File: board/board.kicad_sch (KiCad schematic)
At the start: 10 parts, among them J1 RJ12, J10 PLAN, J2 JST XH, J3 JST XH, J4 RJ12, J5 Barrel_Jack, J6 Seriale, J7 MPX, J8 Conn_02x10_Counter_Clockwise_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, J9 Seriale

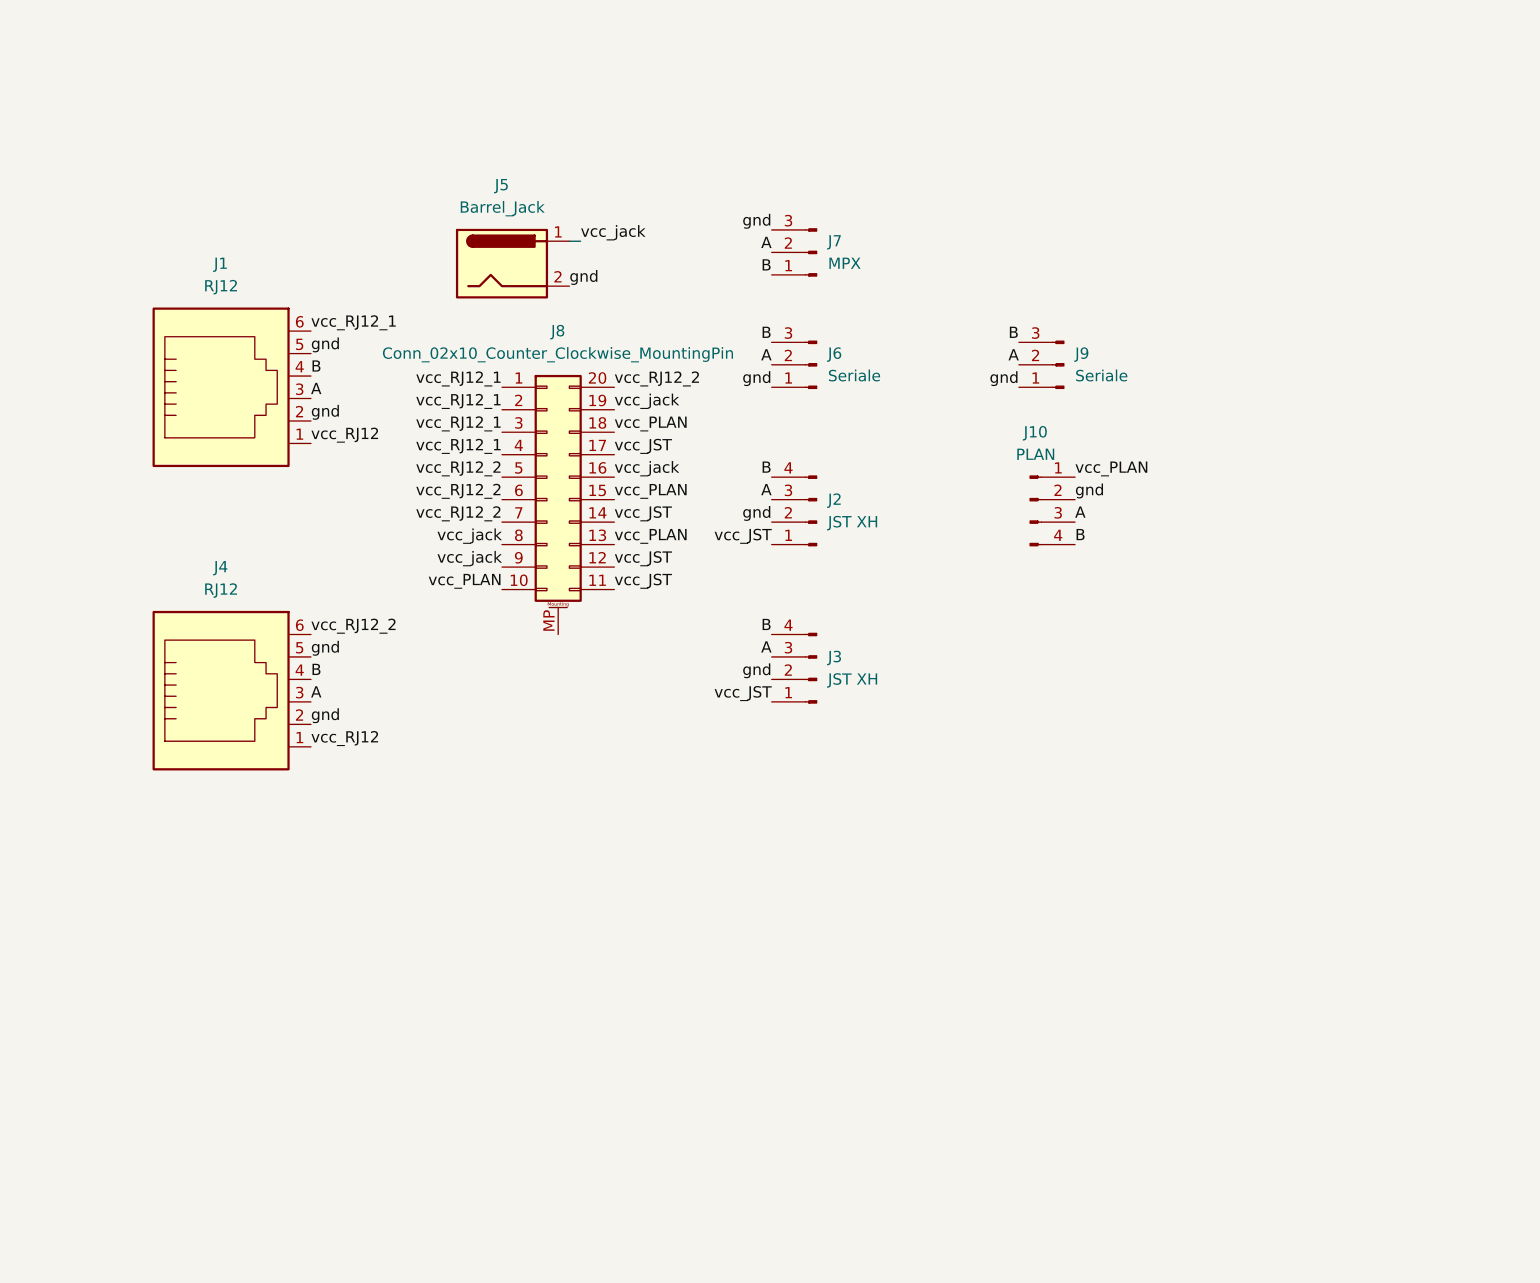
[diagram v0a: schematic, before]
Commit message: [ADD] Add new sockets
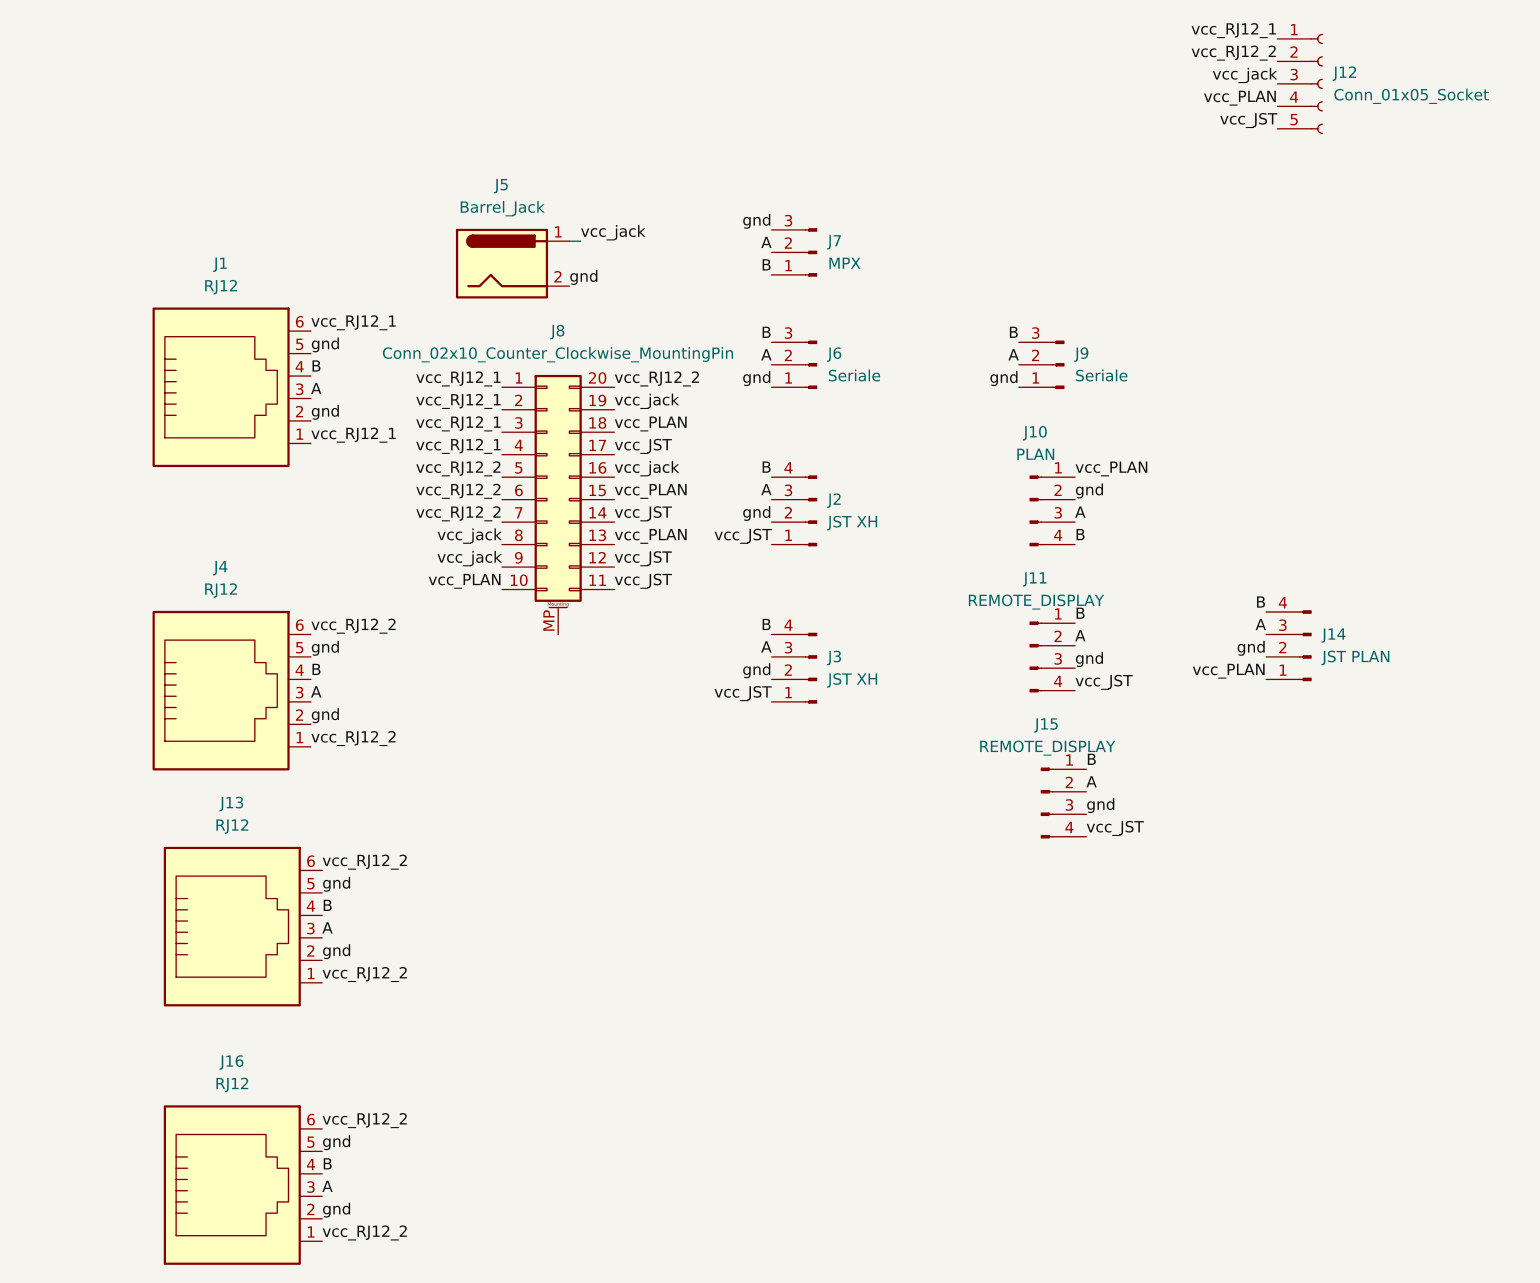
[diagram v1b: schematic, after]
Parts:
- added J11, J15: REMOTE_DISPLAY, board:648104131822, symbol Connector:Conn_01x04_Pin
- added J12: Conn_01x05_Socket, TerminalBlock_Phoenix:TerminalBlock_Phoenix_MPT-0,5-5-2.54_1x05_P2.54mm_Horizontal, symbol Connector:Conn_01x05_Socket
- added J13, J16: RJ12, Connector_RJ:RJ25_Wayconn_MJEA-660X1_Horizontal, symbol Connector:RJ12
- added J14: JST PLAN, Connector_JST:JST_XH_B4B-XH-AM_1x04_P2.50mm_Vertical, symbol Connector:Conn_01x04_Pin
- J5: footprint Connector_BarrelJack:BarrelJack_CUI_PJ-063AH_Horizontal -> Connector_BarrelJack:BarrelJack_GCT_DCJ200-10-A_Horizontal
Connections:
- net A: now also J11.2 (Pin_2), J13.3, J14.3 (Pin_3), J15.2 (Pin_2), J16.3
- net B: now also J11.1 (Pin_1), J13.4, J14.4 (Pin_4), J15.1 (Pin_1), J16.4
- net gnd: now also J11.3 (Pin_3), J13.2, J13.5, J14.2 (Pin_2), J15.3 (Pin_3), J16.2, J16.5
- net vcc_JST: now also J11.4 (Pin_4), J12.5 (Pin_5), J15.4 (Pin_4)
- net vcc_PLAN: now also J12.4 (Pin_4), J14.1 (Pin_1)
- net vcc_RJ12_1: now also J1.1, J12.1 (Pin_1)
- net vcc_RJ12_2: now also J4.1, J12.2 (Pin_2), J13.1, J13.6, J16.1, J16.6
- net vcc_jack: now also J12.3 (Pin_3)
- removed net vcc_RJ12: J1.1, J4.1

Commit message: [UPD] Final version for JLCPCB
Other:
- moved on the sheet: J1, J10, J11, J14, J15, J2, J3, J6, J7, J9
